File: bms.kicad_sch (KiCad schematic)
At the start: 29 parts, among them IC1 MAX77816AEWP+T, Q2 FS8205A, Q4 BSS138, Q5 BSS138, SW8 SW_Slide_DPDT, U12 DW01A, U14 LGS4056HDB, U19 INA238/INA237, U20 AP2112K-1.8

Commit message: neptune 1.3 production
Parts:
- added TP1, TP2, TP3, TP4, TP5, TP6: TestPoint, TestPoint:TestPoint_Pad_1.0x1.0mm, symbol Connector:TestPoint
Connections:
- net +1V8: now also TP1.1
- net +3.3V: now also TP3.1
- net GND: now also TP6.1
- net VCC: now also TP4.1
- net VCCQ: now also TP5.1
- new net +3V0: TP2.1
- no-connect marks 4 -> 5
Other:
- title: (none) -> Neptune On-Board Computer
- moved on the sheet: C33, C50, C51, C52, C53, IC1, L2, Q4, Q5, R43, R44, U20

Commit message: BGA pad size fix v1.4.1
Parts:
- IC1: footprint gaia_obc-footprints:BGA20C40P5X4_213X183X69 -> gaia_obc-footprints:MAXIMBGA20N40P5X4_212X182X69N
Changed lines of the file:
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@@
 			)
 		)
-		(property "Footprint" "gaia_obc-footprints:BGA20C40P5X4_213X183X69"
+		(property "Footprint" "gaia_obc-footprints:MAXIMBGA20N40P5X4_212X182X69N"
 			(at 190.5 130.48 0)
 			(effects

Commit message: obc v1.5
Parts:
- removed IC1: MAX77816AEWP+T, gaia_obc-footprints:MAXIMBGA20N40P5X4_212X182X69N, symbol gaia_obc-symbols:MAX77816AEWP+T
- removed Q4, Q5: BSS138, gaia_obc-footprints:SOT-23, symbol Transistor_FET:BSS138
- removed U20: AP2112K-1.8, gaia_obc-footprints:SOT-23-5, symbol Regulator_Linear:AP2112K-1.8
- added C54: 10uF, Capacitor_SMD:C_0603_1608Metric, symbol Device:C_Small
- added C55, C56, C57: 22uF, Capacitor_SMD:C_0805_2012Metric, symbol Device:C_Small
- added R45: 68.1k, Resistor_SMD:R_0603_1608Metric, symbol Device:R_Small
- added R46: 240k, Resistor_SMD:R_0603_1608Metric, symbol Device:R_Small
- added R47: 100k, Resistor_SMD:R_0603_1608Metric, symbol Device:R_Small
- added U20: ~, gaia_obc-footprints:TPS630701RNMR, symbol gaia_obc-symbols:TPS63070
- C50: value 1uF -> 10uF; footprint Capacitor_SMD:C_0402_1005Metric -> Capacitor_SMD:C_0805_2012Metric
- C51: value 47uF -> 10uF
- C52, C53: value 1uF -> 100nF; footprint Capacitor_SMD:C_0402_1005Metric -> Capacitor_SMD:C_0603_1608Metric
- L2: value 1uH -> 1.5uH; footprint Inductor_SMD:L_Changjiang_FTC201610D -> gaia_obc-footprints:XFL4020152MEC
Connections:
- net 1v8_I2C_1_SCL is gone; now on net VCCQ: R43.2
- net 1v8_I2C_1_SDA is gone; now on net VCCQ: R44.2
- net OBC_BATT is gone; now on net VCCQ: C52.1
- net +3.3V: now also U19.8 (Vbus)
- net GND: now also TP1.1, C54.2, C55.2, C56.2, C57.2, R45.2, U20.10 (PGND), U20.15 (VSEL), U20.4 (GND), U20.6 (FB2)
- net PRI_HI: no longer U19.8 (Vbus)
- net VCC: now also C54.1, C55.1, C56.1, C57.1, R46.1, R47.1, U20.7 (VOUT); no longer C51.1
- net VCCQ: now also C51.1, U20.12 (VIN)
- net at L2.2: now also U20.9 (L2)
- net at L2.1: now also U20.11 (L1)
- removed net +1V8: C53.1, R43.1, R44.1, TP1.1
- new net: R45.1, R46.2, U20.5 (FB)
- new net: R44.1, U20.1 (PS/SYNC)
- new net: R47.2, U20.2 (PG)
- new net: C53.1, U20.3 (VAUX)
- new net: R43.1, U20.14 (EN)
- no-connect marks 5 -> 4
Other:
- note added: "R46 = R45*(VOUT/0.8-1) 240 = 68.1*(3.62/0.8-1)"
- moved on the sheet: TP1, TP2, TP3, TP4, TP5, TP6

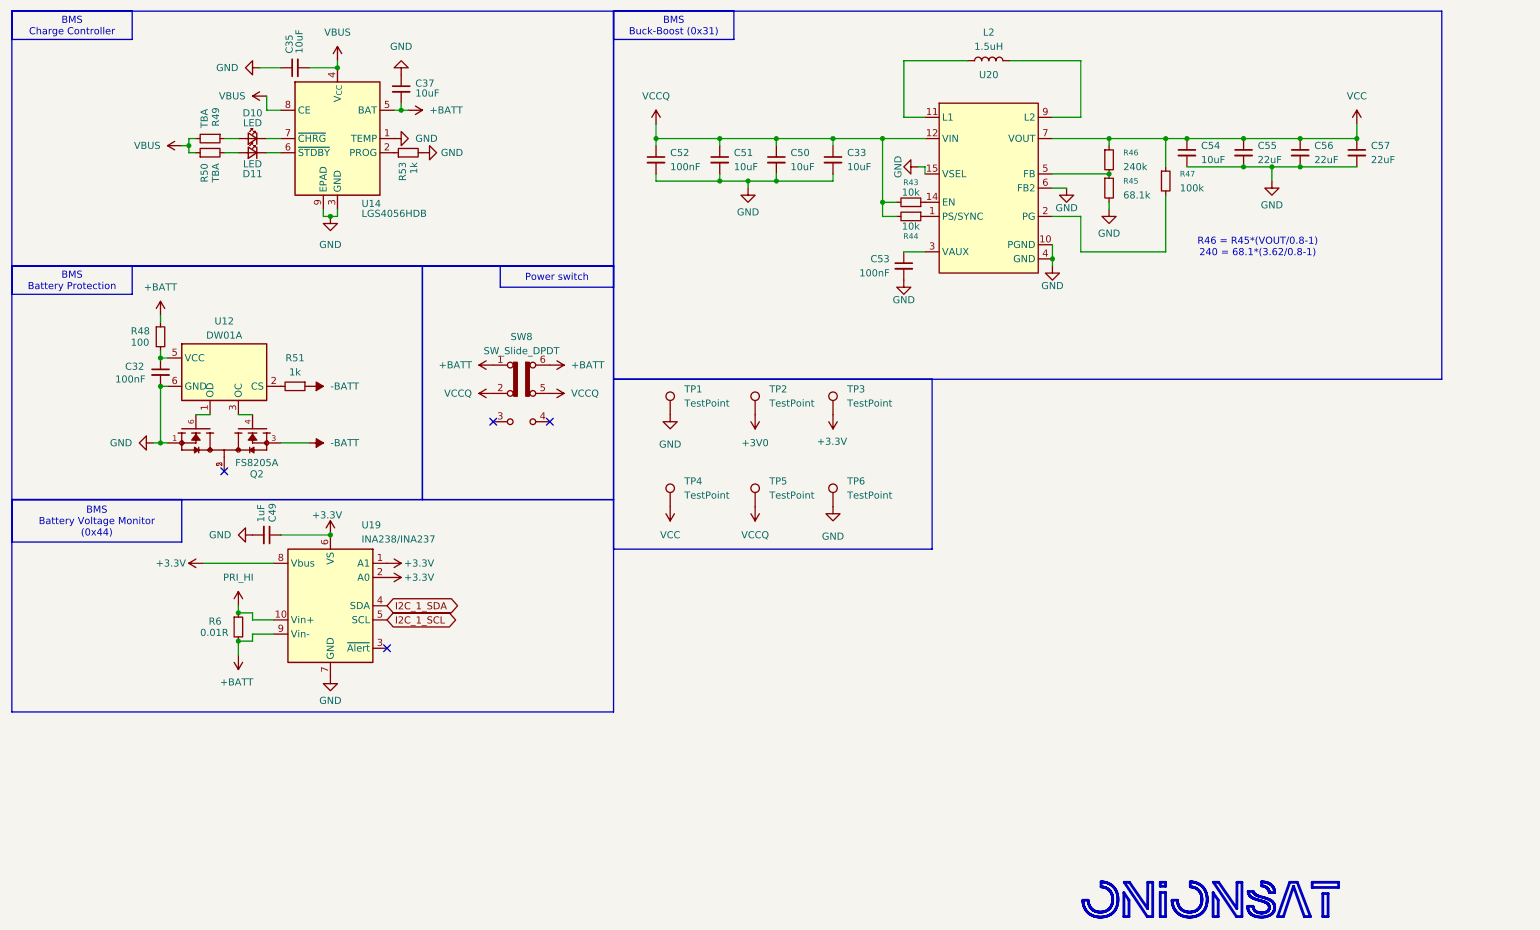
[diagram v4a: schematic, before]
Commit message: Fixing INA238 VBUS err
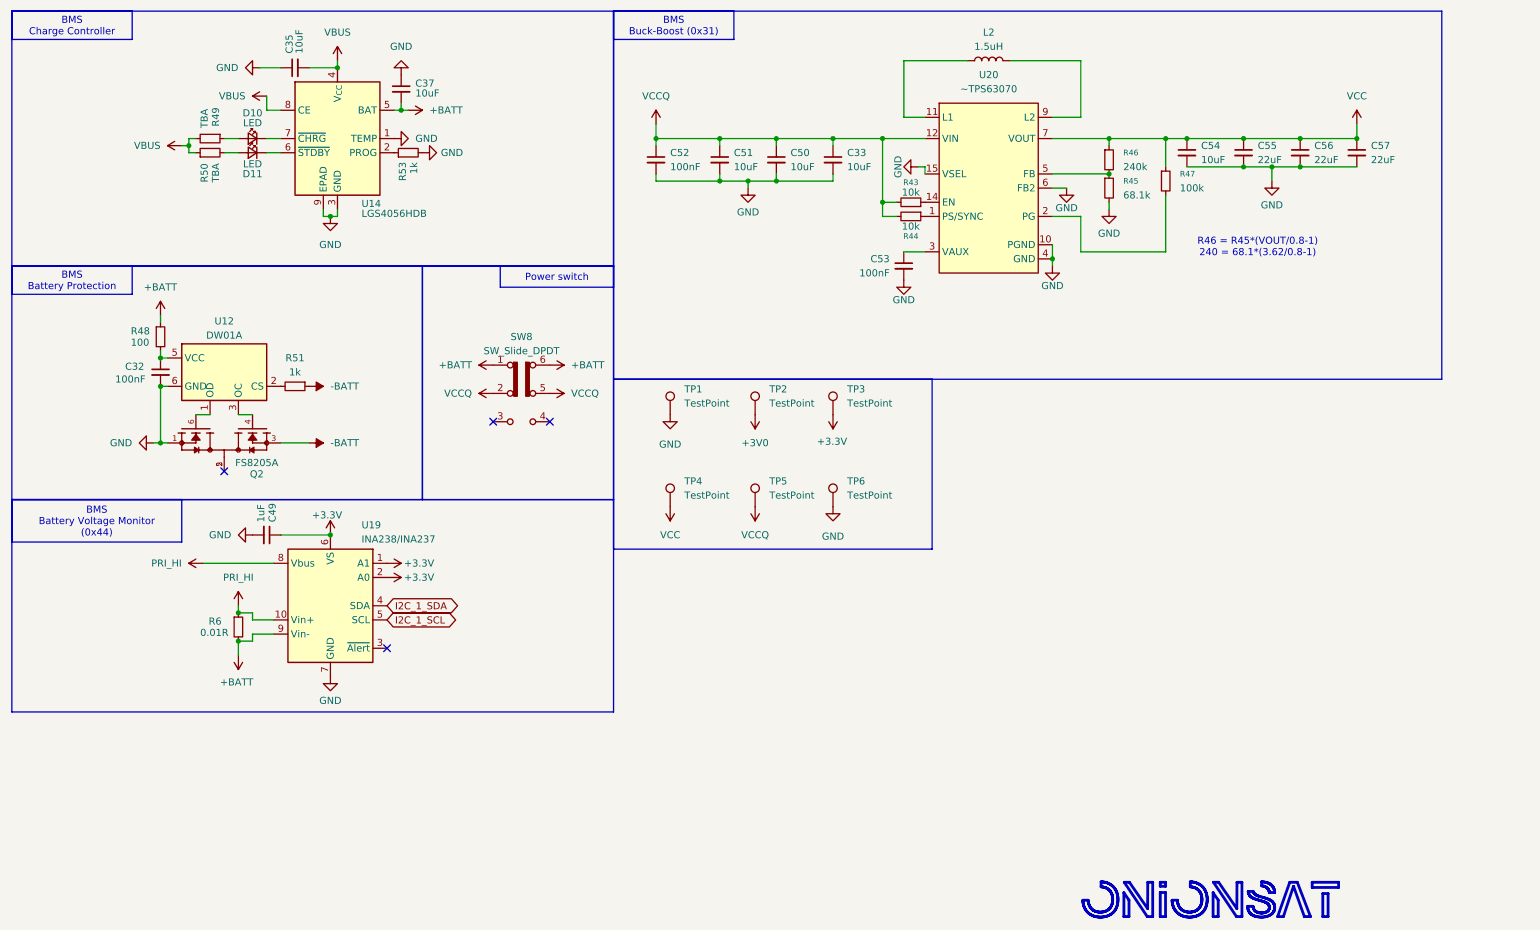
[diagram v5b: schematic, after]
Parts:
- U20: value ~ -> ~TPS63070
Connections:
- net +3.3V: no longer U19.8 (Vbus)
- net PRI_HI: now also U19.8 (Vbus)
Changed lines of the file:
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@@
 	)
 	(symbol
+		(lib_id "power:PRI_HI")
+		(at 48.26 113.03 90)
+		(unit 1)
+		(exclude_from_sim no)
+		(in_bom yes)
+		(on_board yes)
+		(dnp no)
+		(fields_autoplaced yes)
+		(property "Reference" "#PWR0109"
+			(at 52.07 113.03 0)
+			(effects
+				(font
+					(size 1.27 1.27)
+				)
+				(hide yes)
+			)
+		)
+		(property "Value" "PRI_HI"
+			(at 44.45 113.0299 90)
+			(effects
+				(font
+					(size 1.27 1.27)
+				)
+				(justify left)
+			)
+		)
+		(property "Footprint" ""
+			(at 48.26 113.03 0)
+			(effects
+				(font
+					(size 1.27 1.27)
+				)
+				(hide yes)
+			)
+		)
+		(property "Datasheet" ""
+			(at 48.26 113.03 0)
+			(effects
+				(font
+					(size 1.27 1.27)
+				)
+				(hide yes)
+			)
+		)
+		(property "Description" "Power symbol creates a global label with name \"PRI_HI\""
+			(at 48.26 113.03 0)
+			(effects
+				(font
+					(size 1.27 1.27)
+				)
+				(hide yes)
+			)
+		)
+		(pin "1"
+		)
+		(instances
+			(project "gaia_obc"
+				(path "/049f7784-e0f9-4d41-b308-330ac61e4408/fa315d99-9bd8-49b5-8131-f5f6faa8d42e"
+					(reference "#PWR0109")
+					(unit 1)
+				)
+			)
+		)
+	)
+	(symbol
 		(lib_id "power:GND")
 		(at 82.55 36.83 90)
@@
 			)
 		)
-		(property "Value" "~"
+		(property "Value" "~TPS63070"
 			(at 189.23 27.94 0)
 			(effects
@@
 					(unit 1)
 				)
-			)
-		)
-	)
-	(symbol
-		(lib_id "power:+3.3V")
-		(at 48.26 113.03 90)
-		(unit 1)
-		(exclude_from_sim no)
-		(in_bom yes)
-		(on_board yes)
-		(dnp no)
-		(property "Reference" "#PWR0109"
-			(at 52.07 113.03 0)
-			(effects
-				(font
-					(size 1.27 1.27)
-				)
-				(hide yes)
-			)
-		)
-		(property "Value" "+3.3V"
-			(at 45.212 113.03 90)
-			(effects
-				(font
-					(size 1.27 1.27)
-				)
-				(justify left)
-			)
-		)
-		(property "Footprint" ""
-			(at 48.26 113.03 0)
-			(effects
-				(font
-					(size 1.27 1.27)
-				)
-				(hide yes)
-			)
-		)
-		(property "Datasheet" ""
-			(at 48.26 113.03 0)
-			(effects
-				(font
-					(size 1.27 1.27)
-				)
-				(hide yes)
-			)
-		)
-		(property "Description" "Power symbol creates a global label with name \"+3.3V\""
-			(at 48.26 113.03 0)
-			(effects
-				(font
-					(size 1.27 1.27)
-				)
-				(hide yes)
-			)
-		)
-		(pin "1"
-		)
-		(instances
-			(project "gaia_obc"
-				(path "/049f7784-e0f9-4d41-b308-330ac61e4408/fa315d99-9bd8-49b5-8131-f5f6faa8d42e"
-					(reference "#PWR0109")
-					(unit 1)
-				)
